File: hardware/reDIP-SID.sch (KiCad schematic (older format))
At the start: 67 parts, among them J1 Conn_01x01, J2 Conn_01x05, J3 Conn_01x14, J4 Conn_01x10, J5 TYPE-C-31-M-12, J6 Conn_02x05_Odd_Even, SW1 KXT331LHS, U1 NCP115AMX120TCG, U10 ICE40UP5K-SG48I, U2 NCP167AMX330TBG, U3 NCP115AMX120TCG, U4 SN74CBTD16211DGVR, U5 SGTL5000XNLA3, U6 NUF2042XV6, U7 MCP6H01T-E/OT, U8 LY68L6400SLIT, U9 W25Q128JVPIM, X1 ASCO-24.000MHZ-EK-T3

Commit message: Changed to machined (round) pin headers
This allows the board to be mounted directly in a SID socket.

Thanks to @smunaut for the pin header 3D models.
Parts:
- J1: Description CONN HEADER 1 POS .100\" SGL GOLD MATING 5.84mm TAIL 3.05mm -> CONN HDR SQ PIN 0.64mm 1 POS .100\" GOLD MATING 6mm TAIL 3mm; Mfg Sullins -> (none); PN PRPC001SAAN-RC -> (none)
- J2: Description CONN HEADER 5 POS .100\" SGL GOLD MATING 5.84mm TAIL 3.05mm -> CONN HDR SQ PIN 0.64mm 5 POS .100\" GOLD MATING 6mm TAIL 3mm; Mfg Sullins -> (none); PN PRPC005SAAN-RC -> (none)
- J3: footprint reDIP:PinHeader_1x14_P2.54mm_Vertical -> reDIP:PinHeader_1x14_P2.54mm_Vertical_Machined; Description CONN HEADER 14 POS .100\" SGL GOLD MATING 5.84mm TAIL 3.05mm -> CONN HDR ROUND PIN 0.5mm 14 POS .100\" GOLD MATING 3.5mm TA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; Mfg Sullins -> (none); PN PRPC014SAAN-RC -> (none)
- J4: footprint reDIP:PinHeader_1x10_P2.54mm_Vertical -> reDIP:PinHeader_1x10_P2.54mm_Vertical_Machined; Description CONN HEADER 10 POS .100\" SGL GOLD MATING 5.84mm TAIL 3.05mm -> CONN HDR ROUND PIN 0.5mm 10 POS .100\" GOLD MATING 3.5mm TA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; Mfg Sullins -> (none); PN PRPC010SAAN-RC -> (none)
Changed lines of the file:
@@
 F 0 "J4" H 4200 2300 50  0000 C CNN
 F 1 "Conn_01x10" H 4350 2200 50  0001 C CNN
-F 2 "reDIP:PinHeader_1x10_P2.54mm_Vertical" H 4200 2950 50  0001 C CNN
-F 3 "https://drawings-pdf.s3.amazonaws.com/11635.pdf" H 4200 2950 50  0001 C CNN
-F 4 "Sullins" H 4200 2950 50  0001 C CNN "Mfg"
-F 5 "PRPC010SAAN-RC" H 4200 2950 50  0001 C CNN "PN"
-F 6 "CONN HEADER 10 POS .100\" SGL GOLD MATING 5.84mm TAIL 3.05mm" H 4200 2950 50  0001 C CNN "Description"
+F 2 "reDIP:PinHeader_1x10_P2.54mm_Vertical_Machined" H 4200 2950 50  0001 C CNN
+F 3 "" H 4200 2950 50  0001 C CNN
+F 4 "" H 4200 2950 50  0001 C CNN "Mfg"
+F 5 "" H 4200 2950 50  0001 C CNN "PN"
+F 6 "CONN HDR ROUND PIN 0.5mm 10 POS .100\" GOLD MATING 3.5mm TAIL 3mm" H 4200 2950 50  0001 C CNN "Description"
 	1    4200 2950
 	1    0    0    -1
@@
 F 0 "J3" H 5000 1900 50  0000 C CNN
 F 1 "Conn_01x14" H 4918 3476 50  0001 C CNN
-F 2 "reDIP:PinHeader_1x14_P2.54mm_Vertical" H 5000 2750 50  0001 C CNN
-F 3 "https://drawings-pdf.s3.amazonaws.com/11635.pdf" H 5000 2750 50  0001 C CNN
-F 4 "CONN HEADER 14 POS .100\" SGL GOLD MATING 5.84mm TAIL 3.05mm" H 5000 2750 50  0001 C CNN "Description"
-F 5 "Sullins" H 5000 2750 50  0001 C CNN "Mfg"
-F 6 "PRPC014SAAN-RC" H 5000 2750 50  0001 C CNN "PN"
+F 2 "reDIP:PinHeader_1x14_P2.54mm_Vertical_Machined" H 5000 2750 50  0001 C CNN
+F 3 "" H 5000 2750 50  0001 C CNN
+F 4 "CONN HDR ROUND PIN 0.5mm 14 POS .100\" GOLD MATING 3.5mm TAIL 3mm" H 5000 2750 50  0001 C CNN "Description"
+F 5 "" H 5000 2750 50  0001 C CNN "Mfg"
+F 6 "" H 5000 2750 50  0001 C CNN "PN"
 	1    5000 2750
 	-1   0    0    -1
@@
 F 1 "Conn_01x05" H 4280 2151 50  0001 L CNN
 F 2 "reDIP:PinHeader_1x05_P2.54mm_Vertical" H 4200 2250 50  0001 C CNN
-F 3 "https://drawings-pdf.s3.amazonaws.com/11635.pdf" H 4200 2250 50  0001 C CNN
-F 4 "Sullins" H 4200 2250 50  0001 C CNN "Mfg"
-F 5 "PRPC005SAAN-RC" H 4200 2250 50  0001 C CNN "PN"
-F 6 "CONN HEADER 5 POS .100\" SGL GOLD MATING 5.84mm TAIL 3.05mm" H 4200 2250 50  0001 C CNN "Description"
+F 3 "" H 4200 2250 50  0001 C CNN
+F 4 "" H 4200 2250 50  0001 C CNN "Mfg"
+F 5 "" H 4200 2250 50  0001 C CNN "PN"
+F 6 "CONN HDR SQ PIN 0.64mm 5 POS .100\" GOLD MATING 6mm TAIL 3mm" H 4200 2250 50  0001 C CNN "Description"
 	1    4200 2250
 	1    0    0    -1
@@
 F 1 "Conn_01x01" H 4918 1916 50  0001 C CNN
 F 2 "reDIP:PinHeader_1x01_P2.54mm_Vertical" H 5000 2050 50  0001 C CNN
-F 3 "https://drawings-pdf.s3.amazonaws.com/11635.pdf" H 5000 2050 50  0001 C CNN
+F 3 "" H 5000 2050 50  0001 C CNN
 F 4 "" H 5000 2050 50  0001 C CNN "DNP"
-F 5 "CONN HEADER 1 POS .100\" SGL GOLD MATING 5.84mm TAIL 3.05mm" H 5000 2050 50  0001 C CNN "Description"
-F 6 "Sullins" H 5000 2050 50  0001 C CNN "Mfg"
-F 7 "PRPC001SAAN-RC" H 5000 2050 50  0001 C CNN "PN"
+F 5 "CONN HDR SQ PIN 0.64mm 1 POS .100\" GOLD MATING 6mm TAIL 3mm" H 5000 2050 50  0001 C CNN "Description"
+F 6 "" H 5000 2050 50  0001 C CNN "Mfg"
+F 7 "" H 5000 2050 50  0001 C CNN "PN"
 	1    5000 2050
 	-1   0    0    1

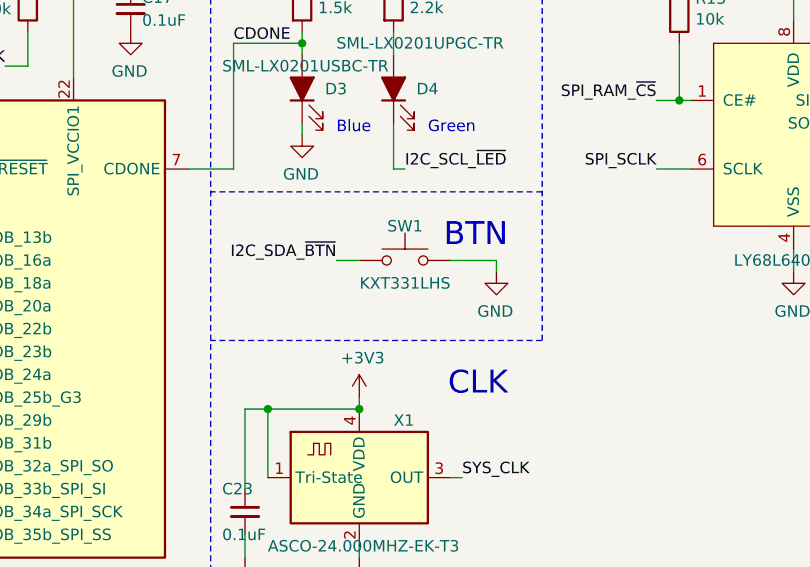
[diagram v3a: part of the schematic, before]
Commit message: Changed from 240gf 100gf button
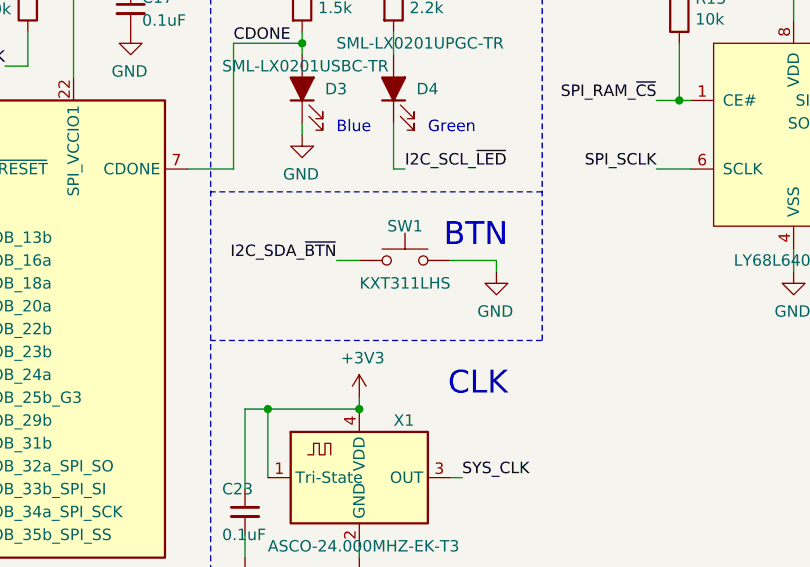
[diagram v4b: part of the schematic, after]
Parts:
- SW1: value KXT331LHS -> KXT311LHS; PN KXT331LHS -> KXT311LHS
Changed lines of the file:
@@
 P 6350 6200
 F 0 "SW1" H 6350 6350 50  0000 C CNN
-F 1 "KXT331LHS" H 6350 6100 50  0000 C CNN
+F 1 "KXT311LHS" H 6350 6100 50  0000 C CNN
 F 2 "CK:SW_SPST_CK_KXT3" H 6350 6400 50  0001 C CNN
 F 3 "https://www.ckswitches.com/media/1465/kxt3.pdf" H 6350 6400 50  0001 C CNN
 F 4 "SW TACT 3.0 x 2.0 mm" H 6350 6200 50  0001 C CNN "Description"
 F 5 "C&K" H 6350 6200 50  0001 C CNN "Mfg"
-F 6 "KXT331LHS" H 6350 6200 50  0001 C CNN "PN"
+F 6 "KXT311LHS" H 6350 6200 50  0001 C CNN "PN"
 	1    6350 6200
 	1    0    0    -1

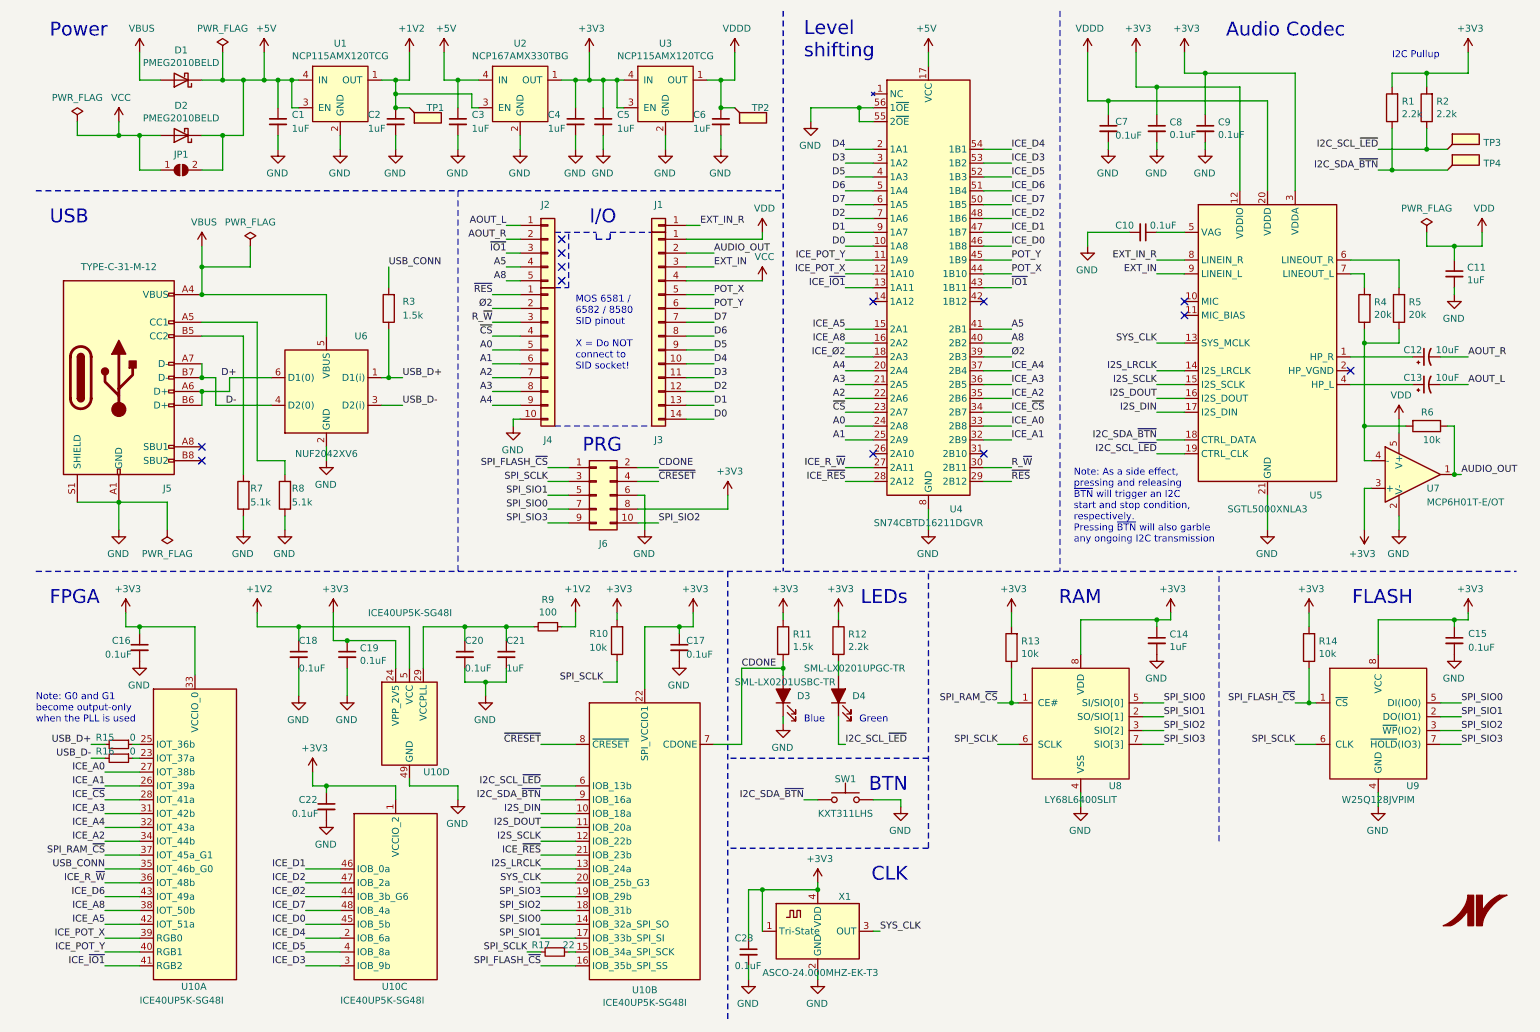
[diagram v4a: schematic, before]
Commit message: Final major changes
* Replaced Schottky diodes with power switch, minimizing 5V rail voltage drop.
* Allow for measurement of VDD on SGTL5000 MIC input, as suggested by @smunaut.
* Adjustments to the USB-C receptacle footprint, based on 2015 and 2020
  HRO TYPE-C-31-M-12 drawings, and the 2019 GCT USB4105 drawing.
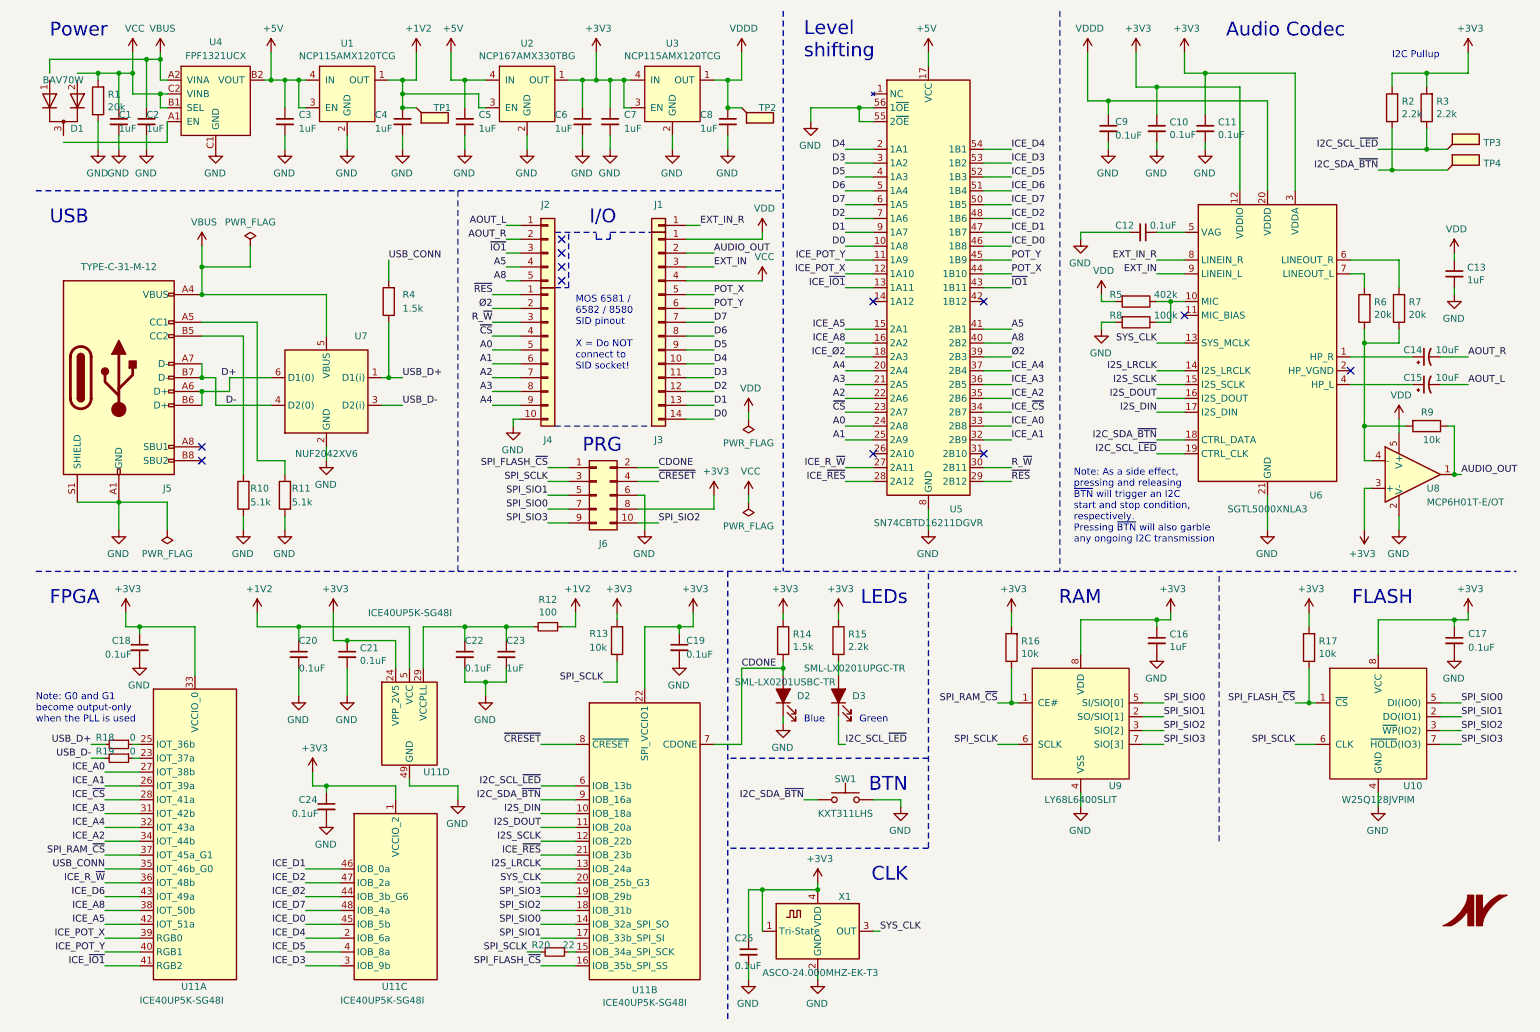
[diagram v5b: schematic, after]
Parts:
- removed D1, D2: PMEG2010BELD, Nexperia:D_SOD-882D, symbol Device:D_Schottky
- removed JP1: SolderJumper_2_Open, reDIP:DNP_0402_1005Metric, symbol Jumper:SolderJumper_2_Open
- added C1, C2: 1uF, Capacitor_SMD:C_0402_1005Metric, symbol Device:C_Small
- added D1: BAV70W, reDIP:SOT-323_SC-70, symbol Nexperia:BAV70W
- added R1: 20k, Resistor_SMD:R_0201_0603Metric, symbol Device:R
- added R5: 402k, Resistor_SMD:R_0201_0603Metric, symbol Device:R
- added R8: 100k, Resistor_SMD:R_0201_0603Metric, symbol Device:R
- added U4: FPF1321UCX, ONSemi:CASE567RM_1.46x0.96mm_P0.5mm, symbol ONSemi:FPF1321UCX
- J5: Notes PIN-IN-PASTE, paste overprinting included in design -> REPLACEMENT PARTS: GCT USB4105
- R13: renamed from R10; Description RES 10kΩ 50mW 5% 0201 -> RES 10kΩ 50mW 1% 0201; PN ERJ-1GNJ103C -> ERJ-1GNF1002C
- R16: renamed from R13; Description RES 10kΩ 50mW 5% 0201 -> RES 10kΩ 50mW 1% 0201; PN ERJ-1GNJ103C -> ERJ-1GNF1002C
- R17: renamed from R14; Description RES 10kΩ 50mW 5% 0201 -> RES 10kΩ 50mW 1% 0201; PN ERJ-1GNJ103C -> ERJ-1GNF1002C
- U1, U2, U3: Mfg ON Semiconductor -> onsemi
- U7: renamed from U6; Mfg ON Semiconductor -> onsemi
- renumbered C8 to C10, C9 to C11, C10 to C12, C11 to C13, C12 to C14, C13 to C15, C14 to C16, C15 to C17, C16 to C18, C17 to C19, C18 to C20, C19 to C21, C20 to C22, C21 to C23, C22 to C24, C23 to C25, C1 to C3, C2 to C4, C3 to C5, C4 to C6, C5 to C7, C6 to C8, C7 to C9, D3 to D2, D4 to D3, R7 to R10, R8 to R11, R9 to R12, R11 to R14, R12 to R15, R15 to R18, R16 to R19, R1 to R2, R17 to R20, R2 to R3, R3 to R4, R4 to R6, R5 to R7, R6 to R9, U9 to U10, U10 to U11, U4 to U5, U5 to U6, U7 to U8, U8 to U9
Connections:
- net +5V: now also U4.B2 (VOUT)
- net GND: now also C1.2, C2.2, R1.1, R8.2, U4.C1 (GND)
- net VBUS: now also C2.1, U4.A2 (VINA)
- net VCC: now also C1.1, R1.2, U4.B1 (SEL), U4.C2 (VINB)
- net VDD: now also R5.2
- net at U6.10 (MIC): now also R5.1, R8.1
- no-connect marks 13 -> 12
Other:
- moved on the sheet: C3, C4, C5, C6, C7, C8, R4, TP1, TP2, U1, U2, U3

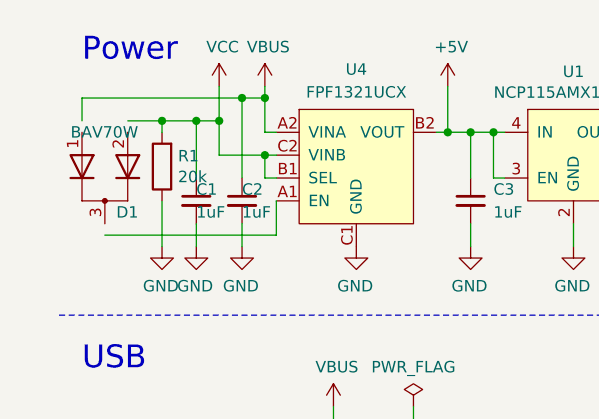
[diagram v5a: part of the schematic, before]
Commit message: Added back JP1
Thanks to @smunaut for the suggestion of jumpering VBUS and VCC
instead of 5V and VCC, making JP1 compatible with the power switch.
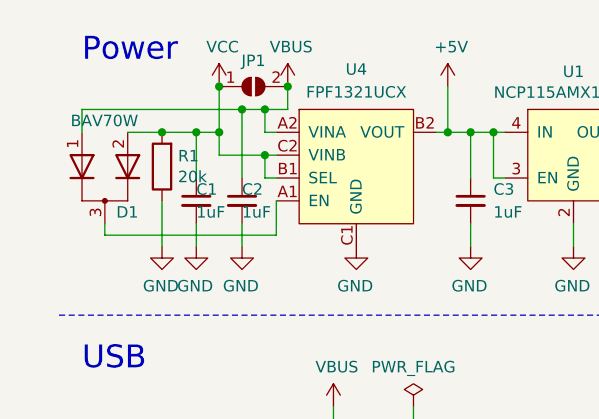
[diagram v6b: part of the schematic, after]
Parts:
- added JP1: SolderJumper_2_Open, reDIP:DNP_0402_1005Metric, symbol Jumper:SolderJumper_2_Open
- J6: Description CONN HEADER 2x5 POS .100\" DBL GOLD MATING 5.84mm TAIL 3.05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 -> CONN HDR SQ PIN 2x5 POS .100\" GOLD MATING 6mm TAIL 3mm; Mfg Sullins -> (none); PN PRPC005DAAN-RC -> (none)
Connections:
- net VBUS: now also D1.1 (A), JP1.2 (B)
- net VCC: now also D1.2 (A), JP1.1 (A)
- net at U4.A1 (EN): now also D1.3 (K)
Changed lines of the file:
@@
 F 2 "reDIP:PinHeader_2x05_P2.54mm_Vertical" H 4550 4000 50  0001 C CNN
 F 3 "https://drawings-pdf.s3.amazonaws.com/11636.pdf" H 4550 4000 50  0001 C CNN
-F 4 "CONN HEADER 2x5 POS .100\" DBL GOLD MATING 5.84mm TAIL 3.05mm" H 4550 4000 50  0001 C CNN "Description"
-F 5 "Sullins" H 4550 4000 50  0001 C CNN "Mfg"
-F 6 "PRPC005DAAN-RC" H 4550 4000 50  0001 C CNN "PN"
+F 4 "CONN HDR SQ PIN 2x5 POS .100\" GOLD MATING 6mm TAIL 3mm" H 4550 4000 50  0001 C CNN "Description"
+F 5 "" H 4550 4000 50  0001 C CNN "Mfg"
+F 6 "" H 4550 4000 50  0001 C CNN "PN"
 F 7 "DNP" H 4550 4000 50  0001 C CNN "DNP"
 	1    4550 4000
@@
 L power:VBUS #PWR02
 U 1 1 612EE4E0
-P 1400 800
-F 0 "#PWR02" H 1400 650 50  0001 C CNN
-F 1 "VBUS" H 1415 973 50  0000 C CNN
-F 2 "" H 1400 800 50  0001 C CNN
-F 3 "" H 1400 800 50  0001 C CNN
-	1    1400 800
+P 1500 800
+F 0 "#PWR02" H 1500 650 50  0001 C CNN
+F 1 "VBUS" H 1515 973 50  0000 C CNN
+F 2 "" H 1500 800 50  0001 C CNN
+F 3 "" H 1500 800 50  0001 C CNN
+	1    1500 800
 	1    0    0    -1
 $EndComp
@@
 	1100 1500 1100 1400
 Wire Wire Line
-	1400 800  1400 850
-Wire Wire Line
 	1200 1100 1400 1100
-Connection ~ 1400 850
-Wire Wire Line
-	1300 850  600  850
-Wire Wire Line
-	1400 850  1300 850
-Connection ~ 1300 850
-Wire Wire Line
-	1300 1200 1300 850
 Wire Wire Line
 	1450 1300 1450 1450
-Wire Wire Line
-	1200 1100 1200 950
-Wire Wire Line
-	1200 950  1100 950
-Connection ~ 1200 950
-Wire Wire Line
-	1200 950  1200 800
-Connection ~ 1100 950
-Wire Wire Line
-	1100 950  950  950
-Wire Wire Line
-	1400 850  1400 1000
 Wire Wire Line
 	2200 800  2200 1000
@@
 P 700 1300
 F 0 "D1" V 650 1250 50  0000 R CNN
-F 1 "BAV70W" V 1000 1450 50  0000 R CNN
+F 1 "BAV70W" V 1050 1450 50  0000 R CNN
 F 2 "reDIP:SOT-323_SC-70" H 700 1300 50  0001 C CNN
 F 3 "https://assets.nexperia.com/documents/data-sheet/BAV70_SER.pdf" V 700 1300 50  0001 C CNN
@@
 $EndComp
 Wire Wire Line
-	1100 950  1100 1200
+	1100 1000 1100 1200
 $Comp
 L Device:C_Small C1
@@
 	1    0    0    -1
 $EndComp
-Wire Wire Line
-	600  850  600  950
-Wire Wire Line
-	950  950  950  1000
-Connection ~ 950  950
-Wire Wire Line
-	950  950  800  950
 $Comp
 L power:GND #PWR014
@@
 Wire Wire Line
 	950  1300 950  1500
+$Comp
+L Jumper:SolderJumper_2_Open JP1
+U 1 1 61EEFC0E
+P 1350 800
+F 0 "JP1" H 1350 913 50  0000 C CNN
+F 1 "SolderJumper_2_Open" H 1350 914 50  0001 C CNN
+F 2 "reDIP:DNP_0402_1005Metric" H 1350 800 50  0001 C CNN
+F 3 "~" H 1350 800 50  0001 C CNN
+F 4 "DNP" H 1350 800 50  0001 C CNN "DNP"
+F 5 "JUMPER" H 1350 800 50  0001 C CNN "Description"
+	1    1350 800
+	1    0    0    -1
+$EndComp
+Connection ~ 1200 800
+Connection ~ 1500 800
+Wire Wire Line
+	1400 900  1300 900
+Wire Wire Line
+	1400 900  1400 1000
+Wire Wire Line
+	600  900  600  1000
+Wire Wire Line
+	1300 1200 1300 900
+Connection ~ 1300 900
+Wire Wire Line
+	1300 900  600  900
+Wire Wire Line
+	1500 900  1400 900
+Wire Wire Line
+	1500 800  1500 900
+Connection ~ 1400 900
+Wire Wire Line
+	1200 800  1200 1000
+Wire Wire Line
+	1200 1000 1100 1000
+Connection ~ 1200 1000
+Wire Wire Line
+	1200 1000 1200 1100
+Connection ~ 950  1000
+Wire Wire Line
+	950  1000 800  1000
+Connection ~ 1100 1000
+Wire Wire Line
+	1100 1000 950  1000
+Wire Wire Line
+	700  1450 700  1400
 $EndSCHEMATC

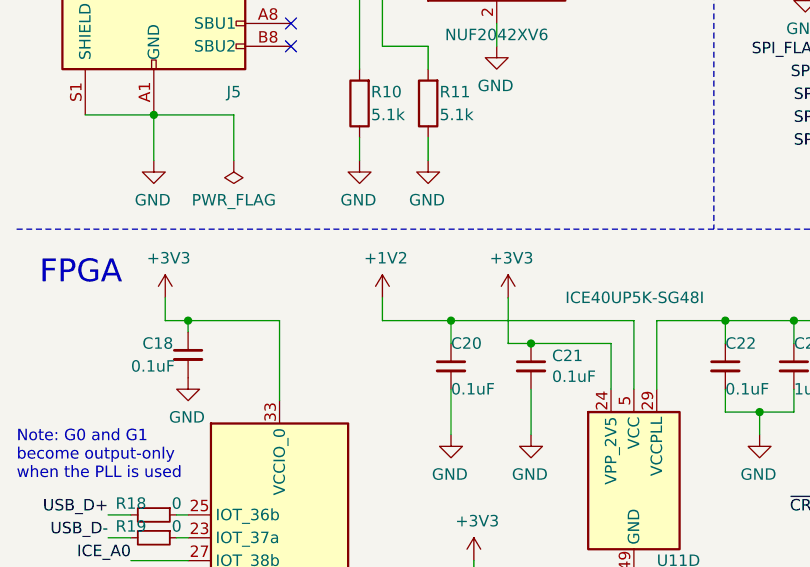
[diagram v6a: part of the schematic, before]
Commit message: Minor adjustments
* Increased hole diameter to 0.65mm for round pin headers
* Minor track and via cleanup
* Changed solder mask color to matte black
* README updates
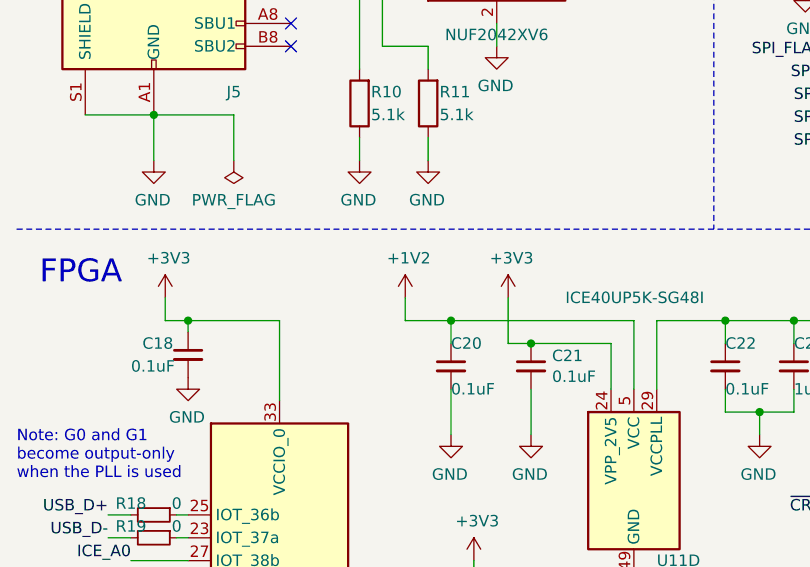
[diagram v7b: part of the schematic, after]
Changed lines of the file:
@@
 L power:+1V2 #PWR053
 U 1 1 5EB96B60
-P 2100 4850
-F 0 "#PWR053" H 2100 4700 50  0001 C CNN
-F 1 "+1V2" H 2115 5023 50  0000 C CNN
-F 2 "" H 2100 4850 50  0001 C CNN
-F 3 "" H 2100 4850 50  0001 C CNN
-	1    2100 4850
+P 2200 4850
+F 0 "#PWR053" H 2200 4700 50  0001 C CNN
+F 1 "+1V2" H 2215 5023 50  0000 C CNN
+F 2 "" H 2200 4850 50  0001 C CNN
+F 3 "" H 2200 4850 50  0001 C CNN
+	1    2200 4850
 	1    0    0    -1
 $EndComp
@@
 	2400 4950 2400 5050
 Wire Wire Line
-	2100 4950 2100 4850
+	2200 4950 2200 4850
 $Comp
 L power:GND #PWR068
@@
 	1    0    0    -1
 $EndComp
-Wire Wire Line
-	2100 4950 2400 4950
 Connection ~ 2400 4950
 Wire Wire Line
@@
 Wire Wire Line
 	700  1450 700  1400
+Wire Wire Line
+	2200 4950 2400 4950
 $EndSCHEMATC
